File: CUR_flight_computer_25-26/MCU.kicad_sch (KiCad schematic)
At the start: 14 parts, among them Y1 ECS-250-18-36B2-CTY

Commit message: updated decoupling
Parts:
- added C25: 1u, symbol Device:C_Small
- added C26, C27: 100n, symbol Device:C_Small
- added FB1: FerriteBead_Small, symbol Device:FerriteBead_Small
- added R28: 47, symbol Device:R_Small_US
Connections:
- net +3.3V: now also FB1.1
- net GND: now also U?.10 (VSS), U?.19 (VSSA), U?.20 (VREF-), U?.27 (VSS), U?.49 (VSS), U?.74 (VSS), U?.99 (VSS), C25.2, C26.2
- net at U?.21 (VREF+): now also C27.1
- net VDDA: now reaches U?.22 (VDDA)
- net VDDA: now also C25.1, C26.1, FB1.2, R28.1
- new net: C27.2, R28.2
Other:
- note added: "See AN5711 Power Supply Management"
- note added: "VDDA Decoupling"
- moved on the sheet: C10, C11, C12, C16, C24, C3, C4, C5, C6, C7, C8, C9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

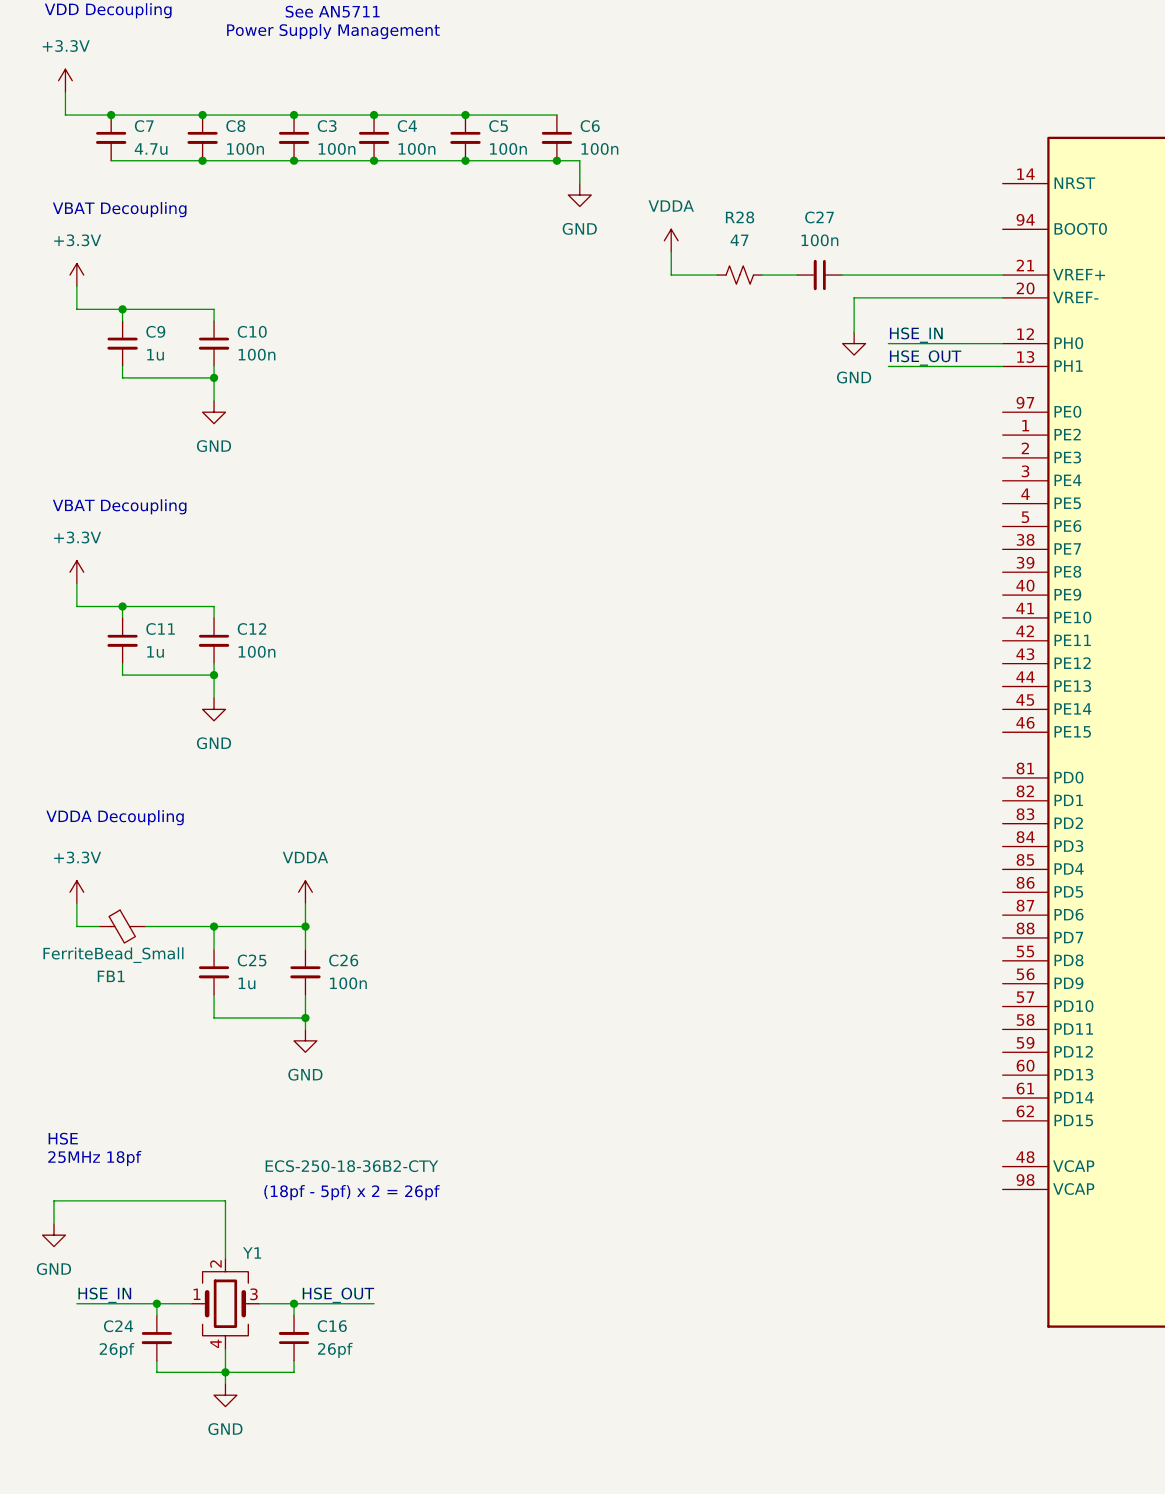
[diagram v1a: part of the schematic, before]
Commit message: added boot and reset buttons
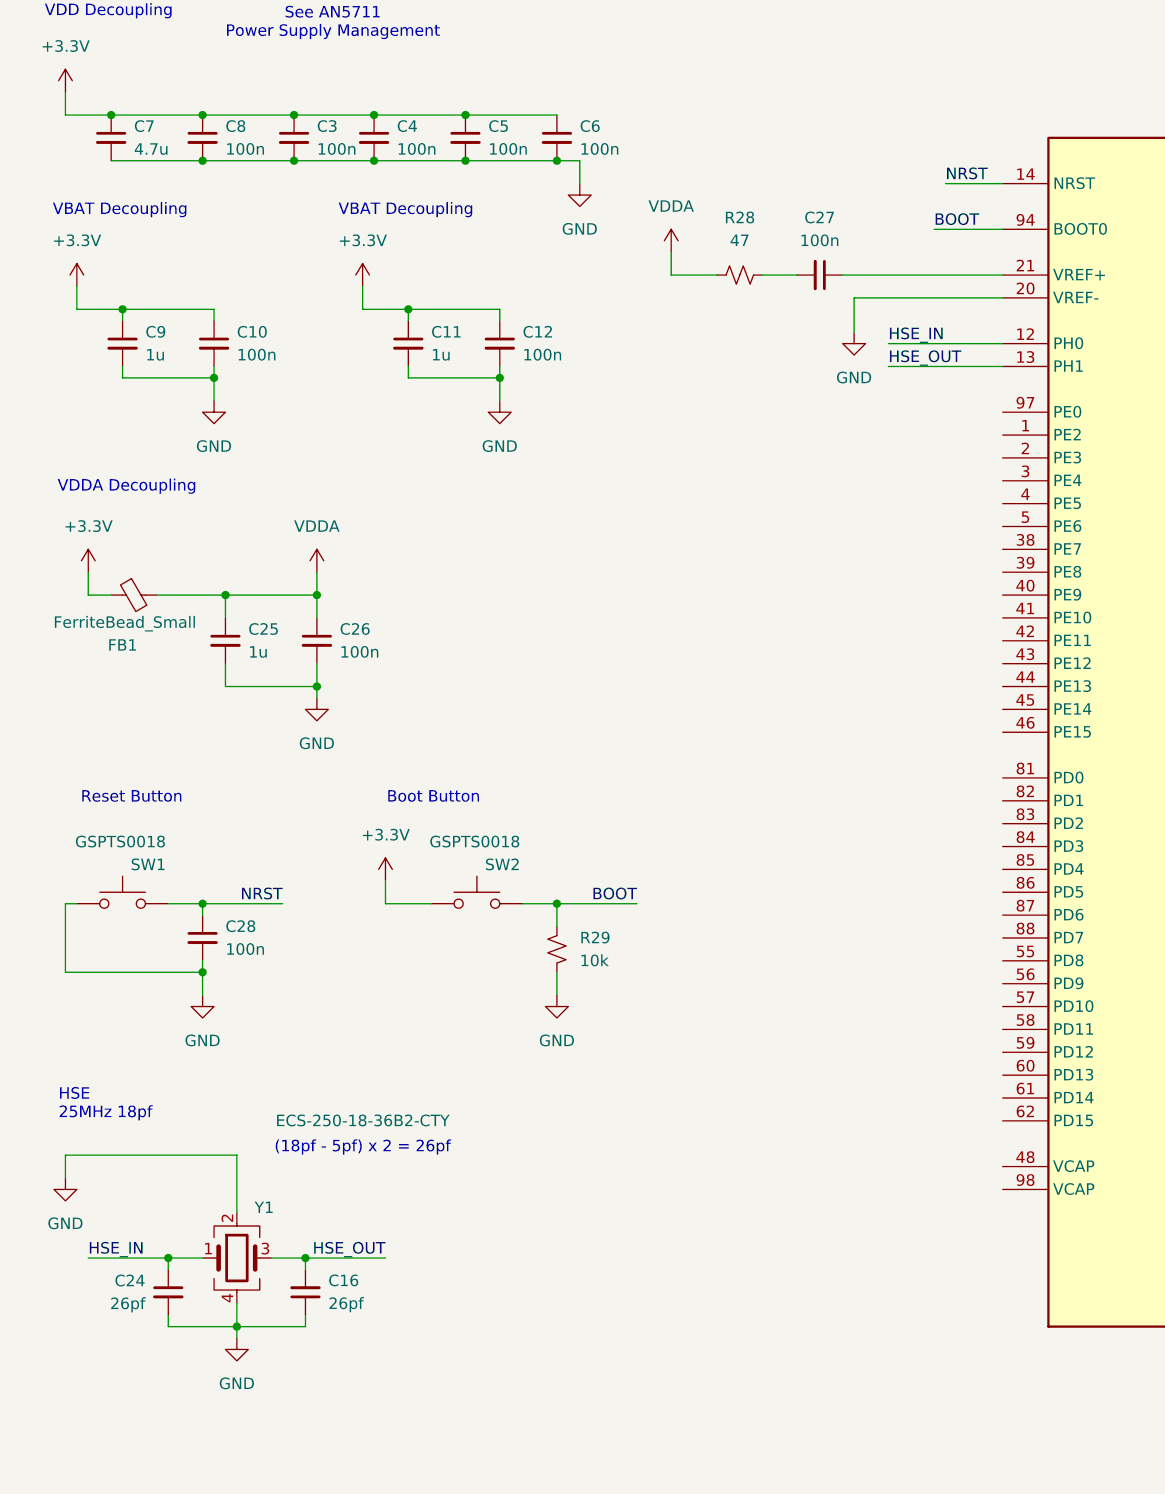
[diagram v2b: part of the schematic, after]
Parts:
- added C28: 100n, symbol Device:C_Small
- added R29: 10k, symbol Device:R_Small_US
- added SW1, SW2: GSPTS0018, PTS815_SJM_250_SMTR_LFS:SW_Push_PTS815_SJM_250_SMTR_LFS, symbol Switch:SW_Push
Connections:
- net +3.3V: now also SW2.2
- net GND: now also C28.2, R29.2, SW1.2
- net NRST: now reaches U?.14 (NRST)
- net NRST: now also C28.1, SW1.1
- net BOOT: now reaches U?.94 (BOOT0)
- net BOOT: now also R29.1, SW2.1
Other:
- note added: "Boot Button"
- note added: "Reset Button"
- moved on the sheet: C11, C12, C16, C24, C25, C26, FB1, Y1

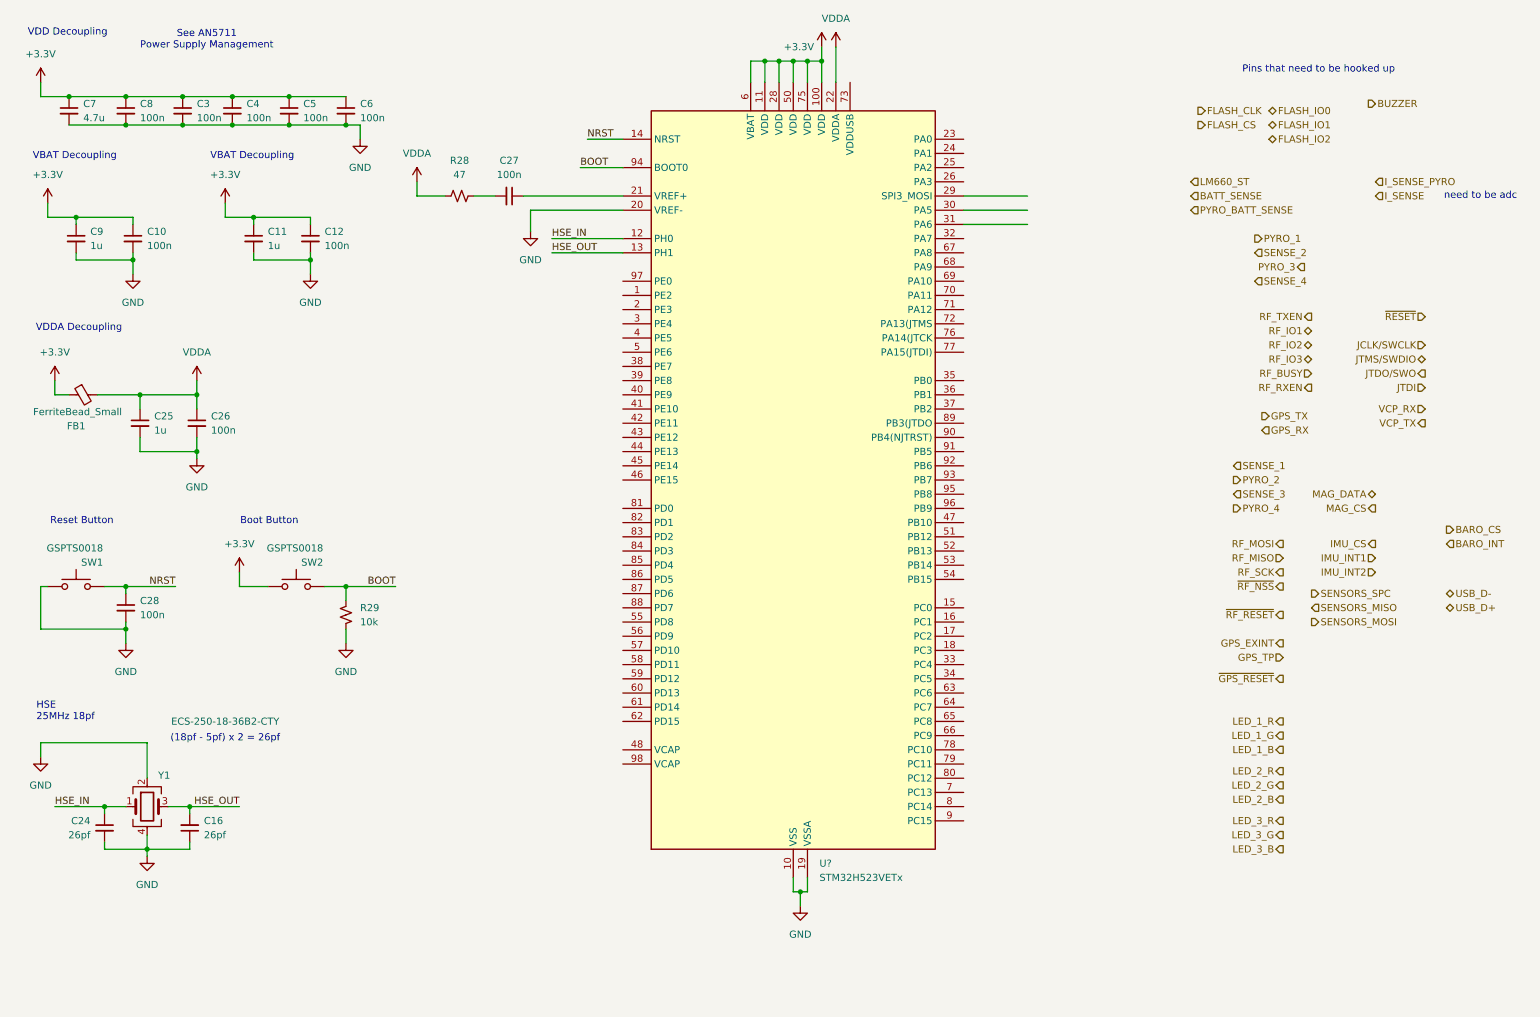
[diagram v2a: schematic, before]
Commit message: changed boot to spdt
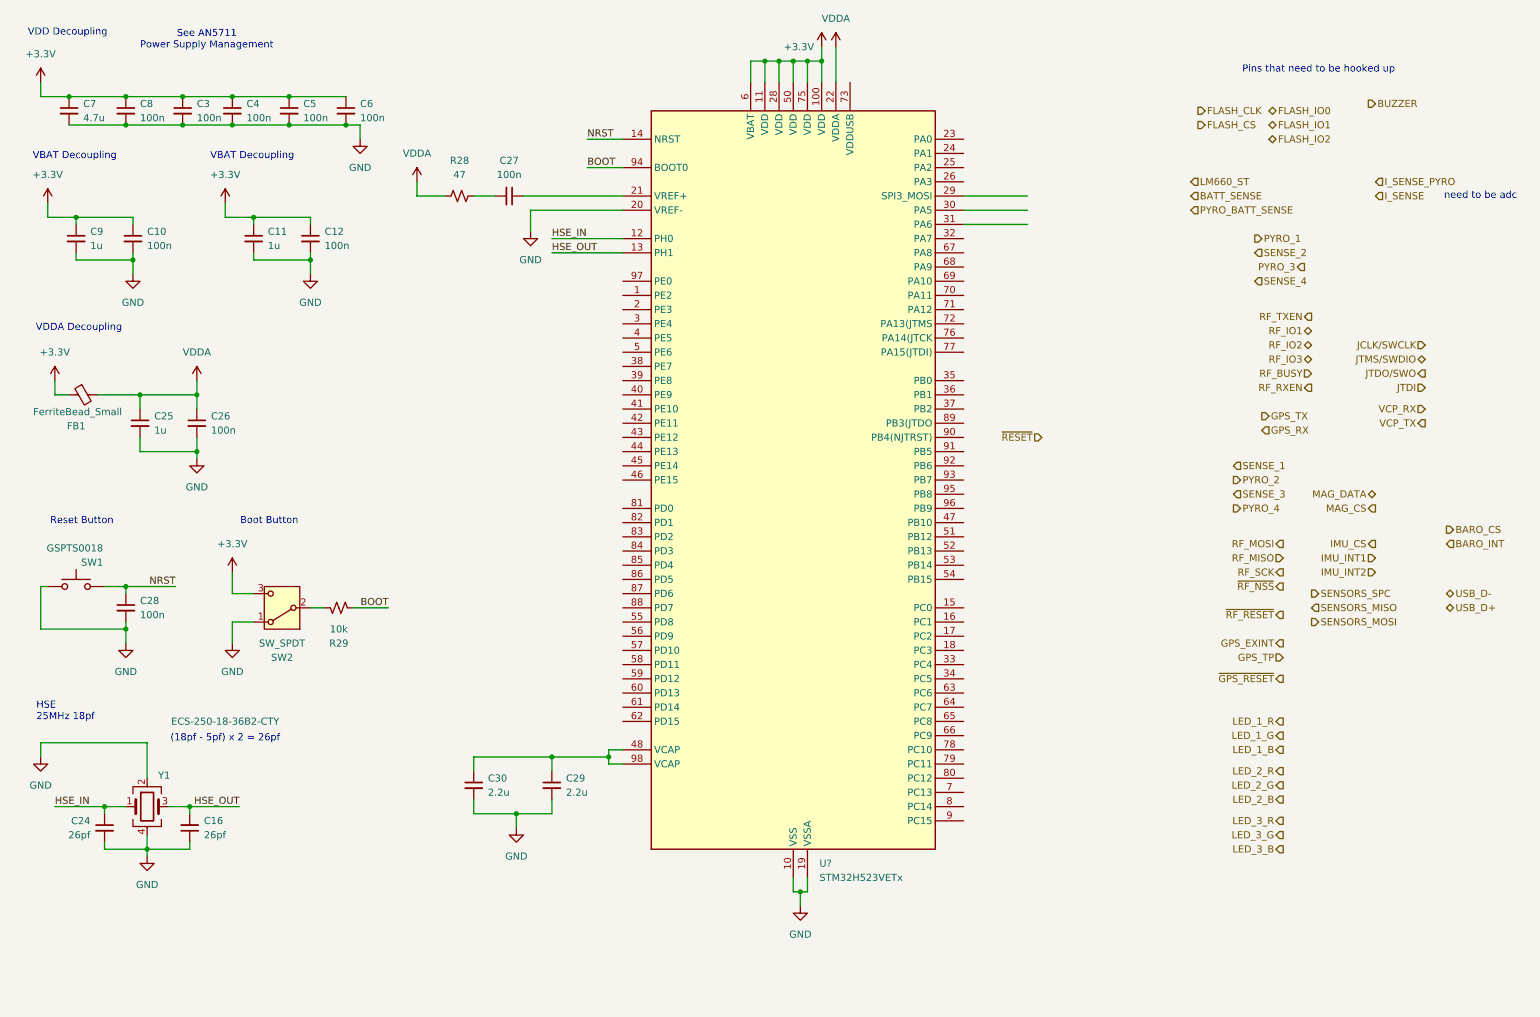
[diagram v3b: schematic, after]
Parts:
- removed SW2: GSPTS0018, PTS815_SJM_250_SMTR_LFS:SW_Push_PTS815_SJM_250_SMTR_LFS, symbol Switch:SW_Push
- added C29, C30: 2.2u, symbol Device:C_Small
- added SW2: SW_SPDT, symbol Switch:SW_SPDT
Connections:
- net +3.3V: now also SW2.3 (C)
- net GND: now also C29.2, C30.2, SW2.1 (A); no longer R29.2
- net at U?.48 (VCAP): now also U?.98 (VCAP), C29.1, C30.1
- new net: R29.2, SW2.2 (B)
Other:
- moved on the sheet: R29

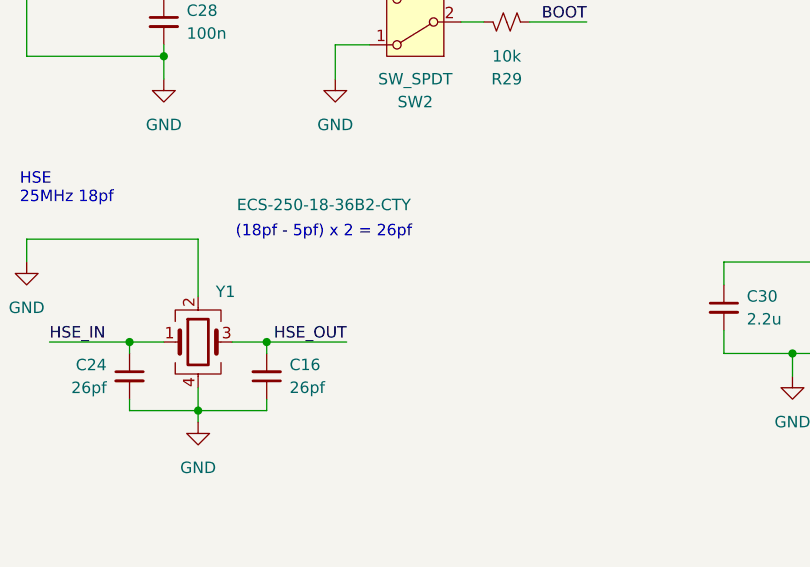
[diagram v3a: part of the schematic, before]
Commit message: added feedback resistor
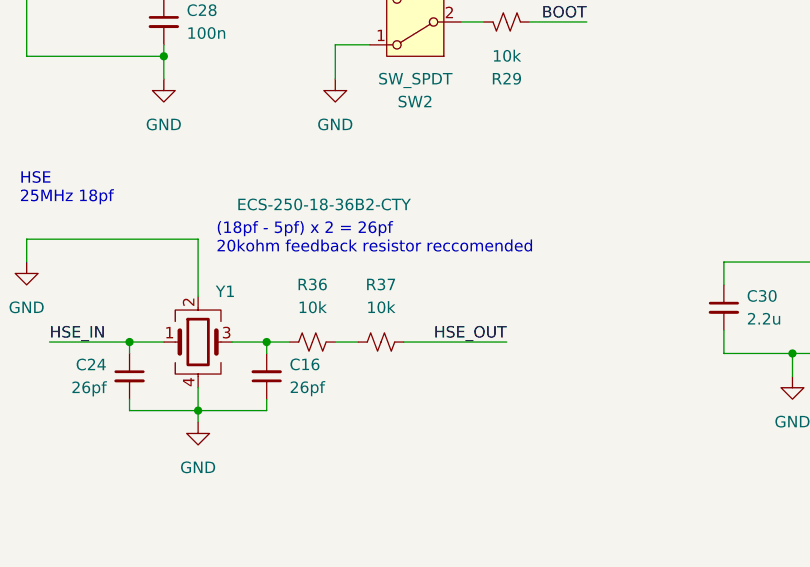
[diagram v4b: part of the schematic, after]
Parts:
- added R36, R37: 10k, symbol Device:R_Small_US
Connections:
- net HSE_OUT: now also R37.1; no longer C16.2, Y1.3
- new net: C16.2, R36.2, Y1.3
- new net: R36.1, R37.2
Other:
- note added: "(18pf - 5pf) x 2 = 26pf 20kohm feedback resistor reccomended"
- note removed: "(18pf - 5pf) x 2 = 26pf"

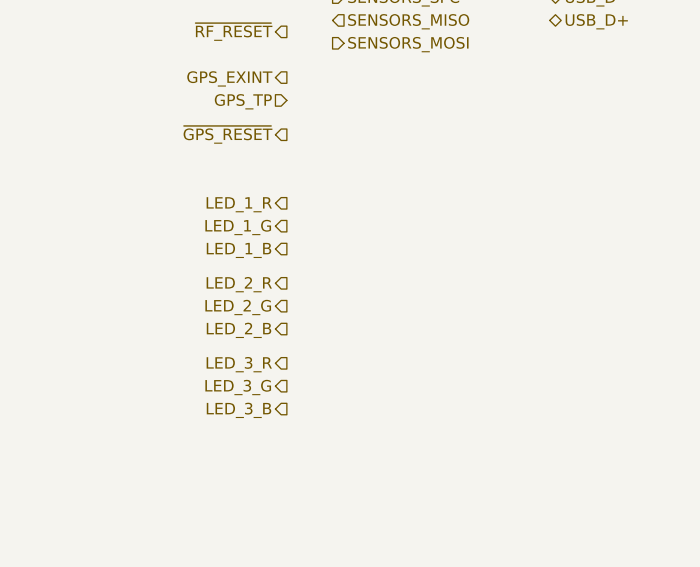
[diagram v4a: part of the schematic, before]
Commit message: added SD_card holder
may need to confirm no pull up resistor required
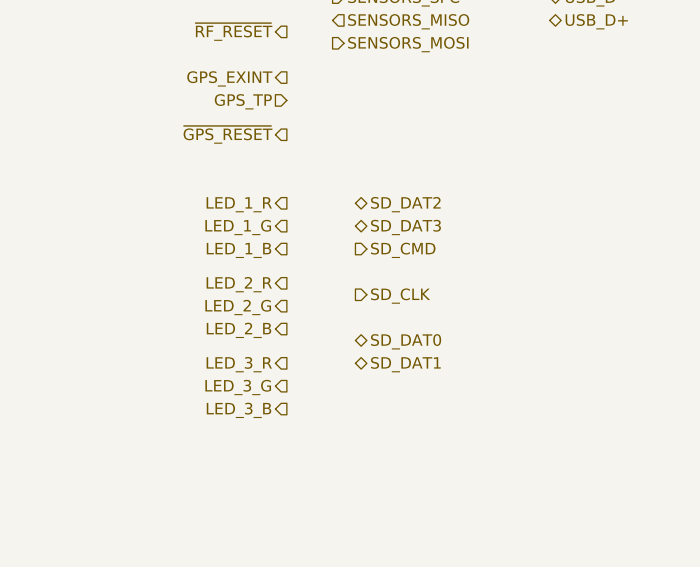
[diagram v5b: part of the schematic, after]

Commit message: organized some stuff
not a lot of actual work here, just organization. Mostly just stopped because I'm going to eat dinner lol
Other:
- note added: "spi buses"
- note added: "unsure if need"
